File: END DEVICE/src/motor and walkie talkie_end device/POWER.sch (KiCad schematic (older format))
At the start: 65 parts, among them IC2 BQ24616RGER, J4 Barrel_Jack_Switch, J5 Motor_Out, J6 BATT_CONN, Q1 DMP6185SE, Q2 DMP6185SE, Q3 FQPF7N65C, Q4 IRF540NPBF, Q5 IRF540NPBF, Q6 DMP6185SE, U6 IRS2128SPBF

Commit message: third commit:very minor changes
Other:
- note added: "Power in= 12V/ 18V(>3A)"
- note added: "TERMINATION CURRENT SETPOINT"
- note removed: "Power in= 12V/ 18V(3A)"
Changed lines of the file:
@@
 ISET2
 Text Notes 1050 4550 0    39   Italic 0
-max fast charge currentt=2.5A
+TERMINATION CURRENT SETPOINT
 Text Label 3450 2900 2    39   Italic 0
 ACSET
@@
 	4800 850  4800 700
 Text Notes 700  1700 0    39   Italic 0
-Power in= 12V/ 18V(3A)
+Power in= 12V/ 18V(>3A)
 $Comp
 L Device:R_US R20

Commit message: commit 4:minor changes
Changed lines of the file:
@@
-	0    1    1    0
-$EndComp
-Wire Wire Line
-	3100 2250 3250 2250
-$Comp
-L power:GND #PWR?
-U 1 1 6185AE66
-P 3100 2250
-AR Path="/6185AE66" Ref="#PWR?"  Part="1"
-AR Path="/615FCEB9/6185AE66" Ref="#PWR0154"  Part="1"
-AR Path="/61DE992E/6185AE66" Ref="#PWR?"  Part="1"
-F 0 "#PWR0154" H 3100 2000 50  0001 C CNN
-F 1 "GND" H 3105 2077 50  0000 C CNN
-F 2 "" H 3100 2250 50  0001 C CNN
-F 3 "" H 3100 2250 50  0001 C CNN
-	1    3100 2250
 	0    1    1    0
 $EndComp
@@
 	1    0    0    -1
 $EndComp
-Wire Wire Line
-	4800 850  4800 700
 Text Notes 700  1700 0    39   Italic 0
 Power in= 12V/ 18V(>3A)
@@
 Text GLabel 9150 1300 2    50   Input ~ 10
 TO_SYS
+Wire Wire Line
+	4800 700  4800 850
+$Comp
+L power:PWR_FLAG #FLG0105
+U 1 1 62374A60
+P 4800 1400
+F 0 "#FLG0105" H 4800 1475 50  0001 C CNN
+F 1 "PWR_FLAG" H 4500 1600 50  0000 L CNN
+F 2 "" H 4800 1400 50  0001 C CNN
+F 3 "~" H 4800 1400 50  0001 C CNN
+	1    4800 1400
+	0    -1   -1   0
+$EndComp
+Wire Wire Line
+	2400 2250 2400 1950
+Wire Wire Line
+	2400 1950 1850 1950
+Wire Wire Line
+	2400 2250 3250 2250
 $EndSCHEMATC

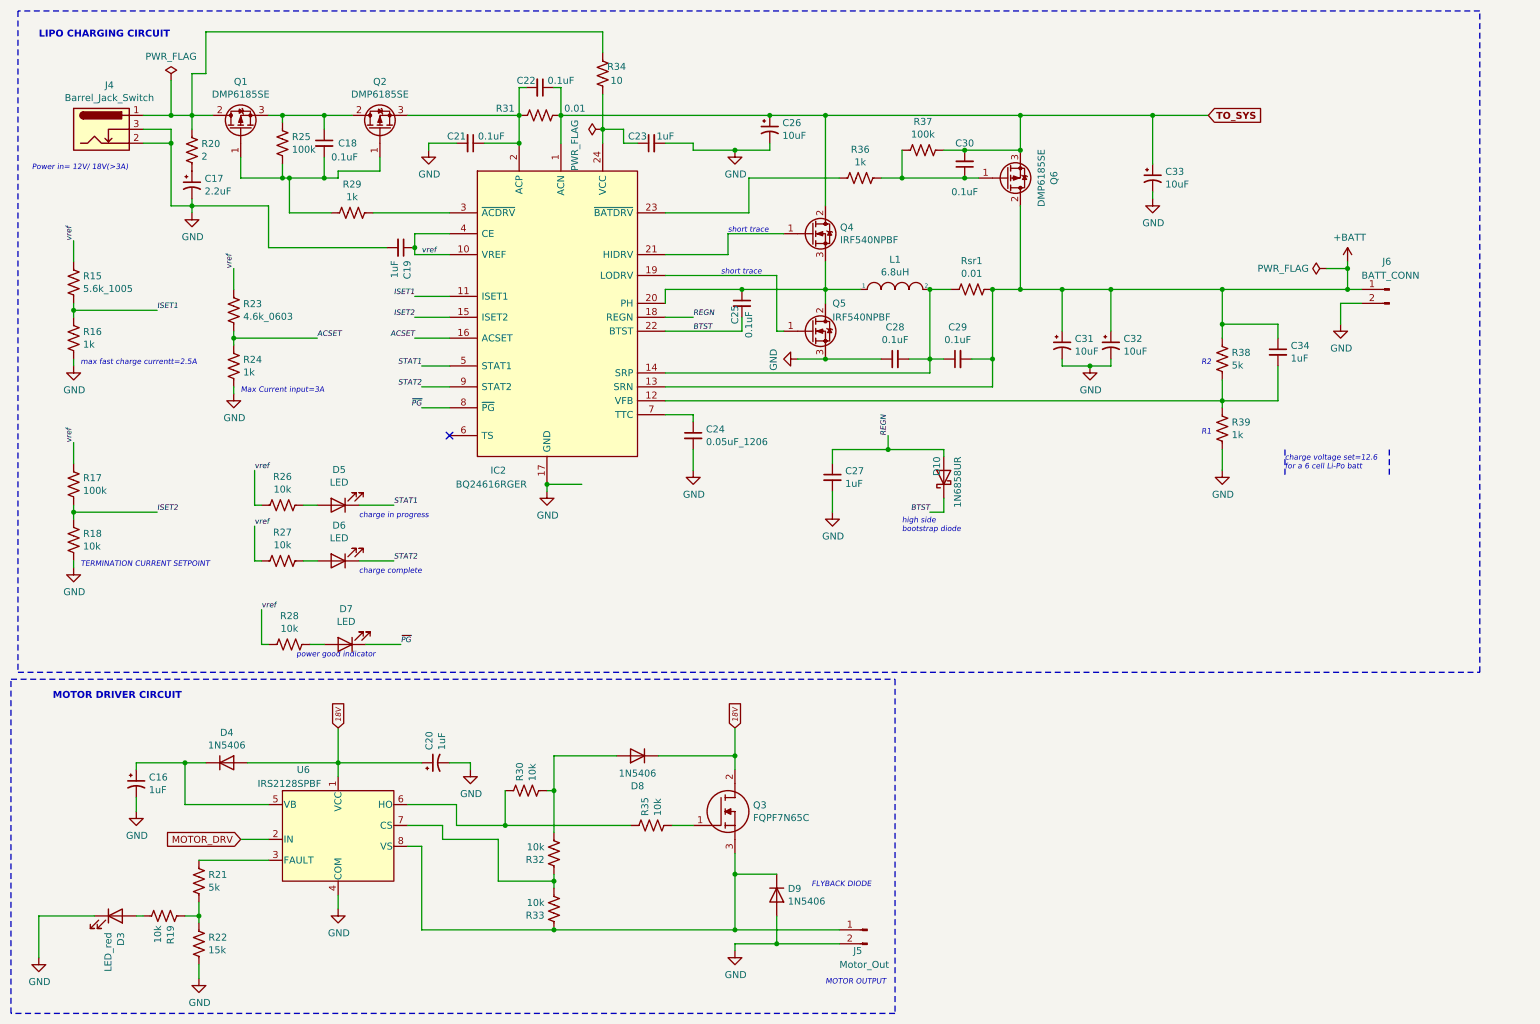
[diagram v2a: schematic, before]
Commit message: All footprint associations updated
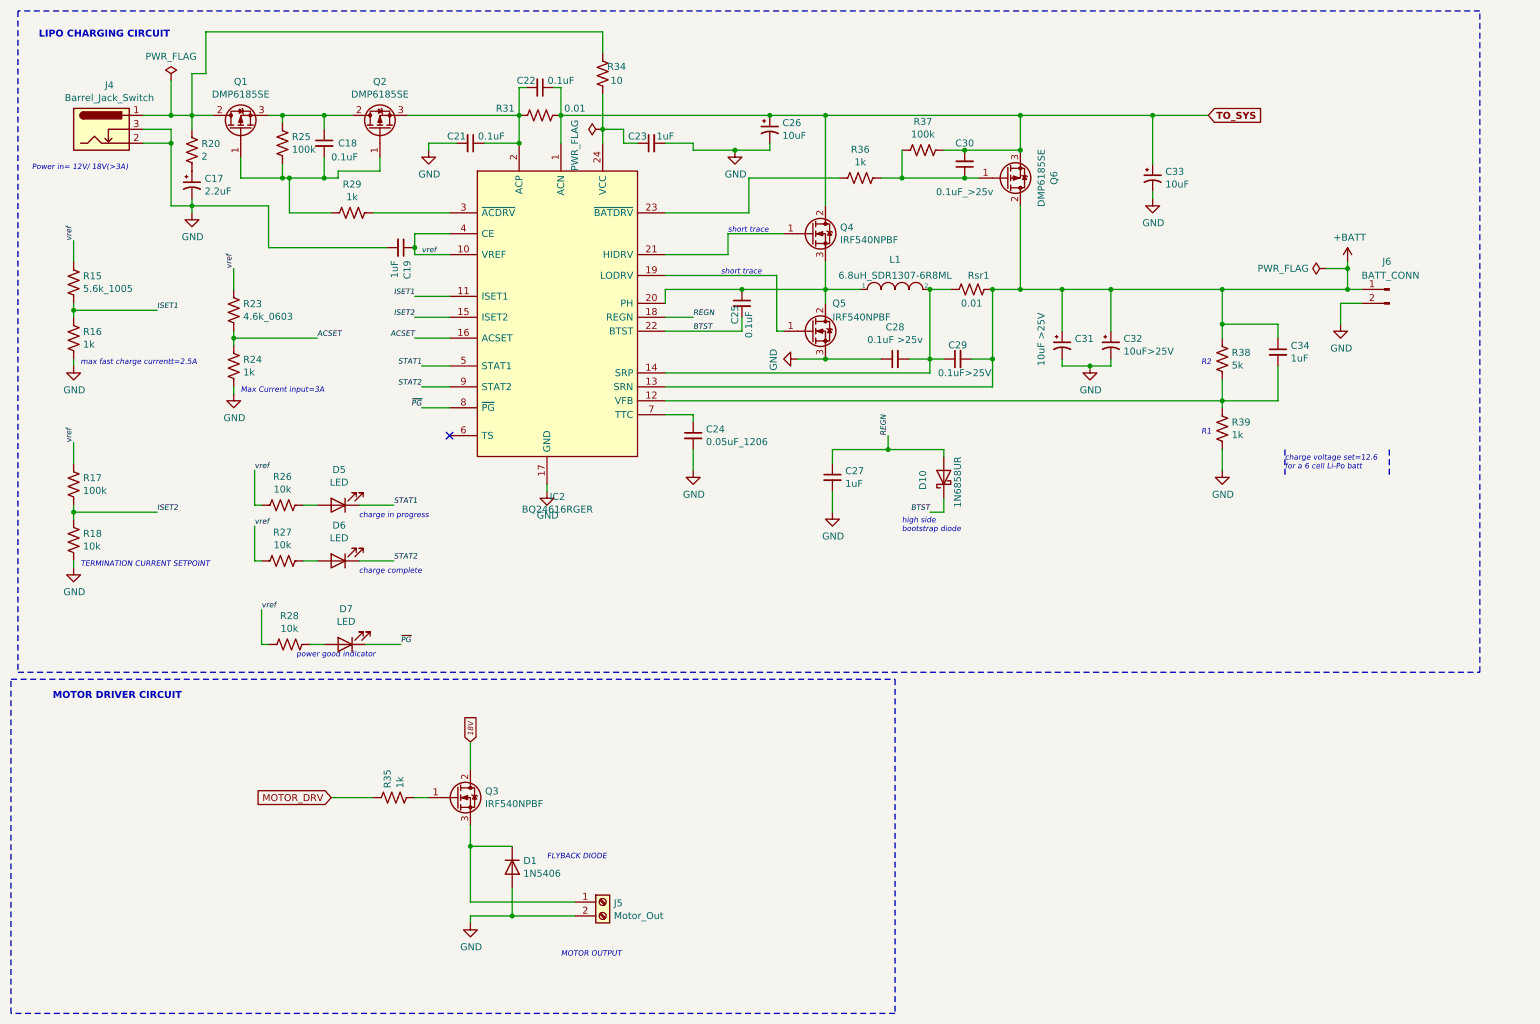
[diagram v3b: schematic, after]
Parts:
- removed C16, C20: 1uF, symbol Device:CP1_Small
- removed D3: LED_red, symbol Device:LED
- removed D4, D8, D9: 1N5406, Diode_THT:D_DO-201AD_P15.24mm_Horizontal, symbol Diode:1N5406
- removed J5: Motor_Out, symbol Connector:Conn_01x02_Male
- removed Q3: FQPF7N65C, TO254P490X1016X1990-3P, symbol SamacSys_Parts:FQPF7N65C
- removed R19, R30, R32, R33: 10k, symbol Device:R_US
- removed R21: 5k, symbol Device:R_US
- removed R22: 15k, symbol Device:R_US
- removed U6: IRS2128SPBF, symbol remote_devices:IRS2128SPBF
- added D1: 1N5406, Diode_THT:D_DO-201AD_P15.24mm_Horizontal, symbol Diode:1N5406
- added J5: Motor_Out, TerminalBlock:TerminalBlock_Altech_AK300-2_P5.00mm, symbol Connector:Screw_Terminal_01x02
- added Q3: IRF540NPBF, Package_TO_SOT_THT:TO-220-3_Vertical, symbol Transistor_FET:IRF540N
- C17, C26, C33: footprint (none) -> Capacitor_Tantalum_SMD:CP_EIA-2012-12_Kemet-R
- C18, C19, C21, C22, C23, C24, C25, C27, C34: footprint (none) -> Capacitor_SMD:C_0603_1608Metric
- C28: value 0.1uF -> 0.1uF >25v; footprint (none) -> Capacitor_SMD:C_0603_1608Metric
- C29: value 0.1uF -> 0.1uF>25V; footprint (none) -> Capacitor_SMD:C_0603_1608Metric
- C30: value 0.1uF -> 0.1uF_>25v; footprint (none) -> Capacitor_SMD:C_0603_1608Metric
- C31: value 10uF -> 10uF >25V; footprint (none) -> Capacitor_Tantalum_SMD:CP_EIA-1608-10_AVX-L
- C32: value 10uF -> 10uF>25V; footprint (none) -> Capacitor_Tantalum_SMD:CP_EIA-1608-10_AVX-L
- D5, D6, D7: footprint (none) -> LED_SMD:LED_0603_1608Metric
- IC2: footprint QFN50P400X400X100-25N-D -> Package_DFN_QFN:QFN-24-1EP_4x4mm_P0.5mm_EP2.6x2.6mm_ThermalVias
- J4: footprint (none) -> Connector_BarrelJack:BarrelJack_Horizontal
- J6: footprint (none) -> Connector_JST:JST_PH_B2B-PH-K_1x02_P2.00mm_Vertical
- L1: value 6.8uH -> 6.8uH_SDR1307-6R8ML; footprint (none) -> Remote_devices:SDR1307680KL
- Q1, Q2, Q6: footprint Package_SON:Diodes_PowerDI3333-8 -> Package_TO_SOT_SMD:SOT-223
- R15: footprint (none) -> Resistor_SMD:R_0402_1005Metric_Pad0.72x0.64mm_HandSolder
- R16, R17, R18, R20, R23, R24, R25, R26, R27, R28, R29, R31, R34, R36, R37, R38, R39, Rsr1: footprint (none) -> Resistor_SMD:R_0603_1608Metric
- R35: value 10k -> 1k; footprint (none) -> Resistor_SMD:R_0603_1608Metric
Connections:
- net 18V: now also Q3.2 (D)
- net GND: now also D1.2 (A), J5.2 (Pin_2)
- net MOTOR_DRV: now also R35.2
- net at R35.1: now also Q3.1 (G)
- new net: D1.1 (K), J5.1 (Pin_1), Q3.3 (S)
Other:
- moved on the sheet: R35

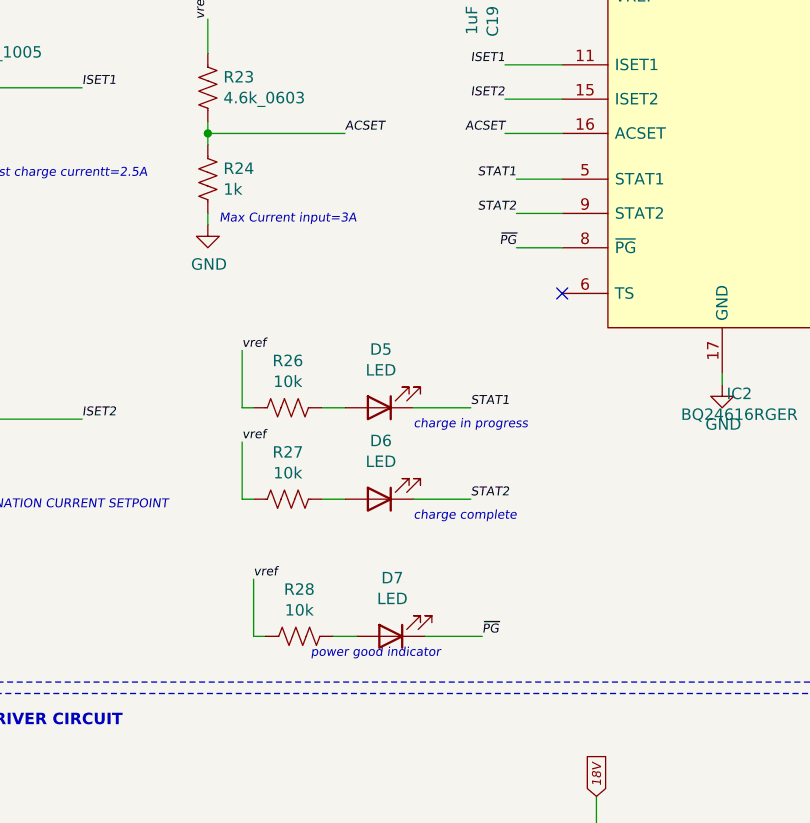
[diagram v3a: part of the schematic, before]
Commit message: Version 2 compressed board
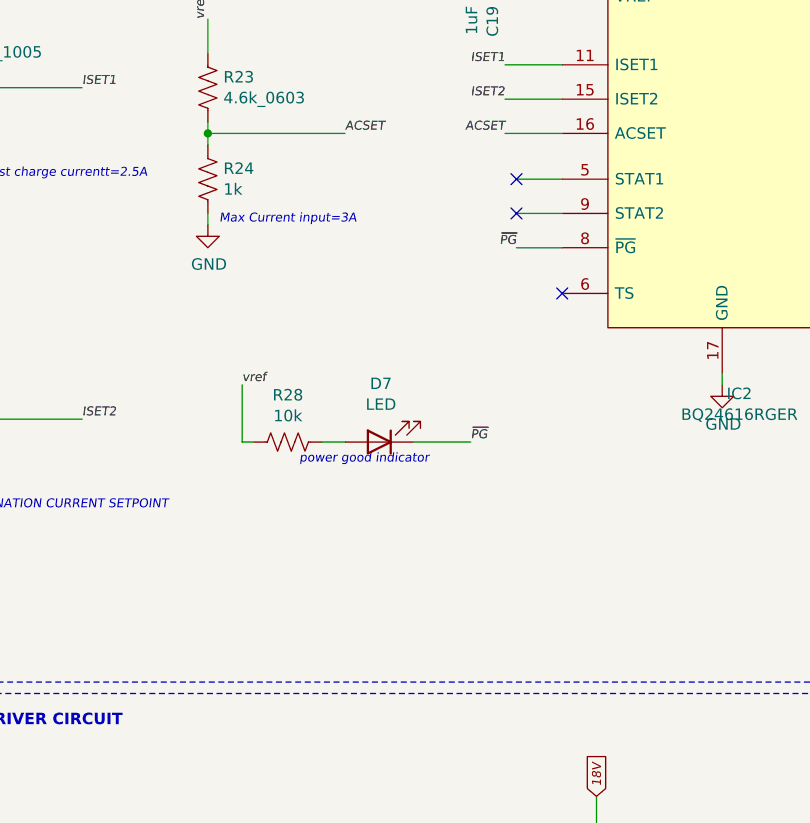
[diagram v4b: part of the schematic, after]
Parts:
- removed D5, D6: LED, LED_SMD:LED_0603_1608Metric, symbol Device:LED
- removed R26, R27: 10k, Resistor_SMD:R_0603_1608Metric, symbol Device:R_US
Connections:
- net STAT1: no longer names the net of IC2.5 (STAT1)
- net STAT2: no longer names the net of IC2.9 (STAT2)
- no-connect marks 1 -> 3
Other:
- note removed: "charge complete"
- note removed: "charge in progress"
- moved on the sheet: D7, R28
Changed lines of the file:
@@
 Text Label 3500 2300 0    39   Italic 0
 vref
-Text Label 2350 4850 0    39   Italic 0
+Text Label 2300 4000 0    39   Italic 0
 vref
 $Comp
 L Device:R_US R28
 U 1 1 617905B6
-P 2550 5100
+P 2500 4250
 AR Path="/615FCEB9/617905B6" Ref="R28"  Part="1"
 AR Path="/61DE992E/617905B6" Ref="R?"  Part="1"
-F 0 "R28" V 2345 5100 50  0000 C CNN
-F 1 "10k" V 2436 5100 50  0000 C CNN
-F 2 "Resistor_SMD:R_0603_1608Metric" V 2590 5090 50  0001 C CNN
-F 3 "~" H 2550 5100 50  0001 C CNN
-	1    2550 5100
+F 0 "R28" V 2295 4250 50  0000 C CNN
+F 1 "10k" V 2386 4250 50  0000 C CNN
+F 2 "Resistor_SMD:R_0603_1608Metric" V 2540 4240 50  0001 C CNN
+F 3 "~" H 2500 4250 50  0001 C CNN
+	1    2500 4250
 	0    1    1    0
 $EndComp
 Wire Wire Line
-	2350 4850 2350 5100
-Wire Wire Line
-	2350 5100 2400 5100
+	2300 4000 2300 4250
+Wire Wire Line
+	2300 4250 2350 4250
 $Comp
 L Device:LED D7
 U 1 1 61799560
-P 2950 5100
+P 2900 4250
 AR Path="/615FCEB9/61799560" Ref="D7"  Part="1"
 AR Path="/61DE992E/61799560" Ref="D?"  Part="1"
-F 0 "D7" H 2943 4845 50  0000 C CNN
-F 1 "LED" H 2943 4936 50  0000 C CNN
-F 2 "LED_SMD:LED_0603_1608Metric" H 2950 5100 50  0001 C CNN
-F 3 "~" H 2950 5100 50  0001 C CNN
-	1    2950 5100
+F 0 "D7" H 2893 3995 50  0000 C CNN
+F 1 "LED" H 2893 4086 50  0000 C CNN
+F 2 "LED_SMD:LED_0603_1608Metric" H 2900 4250 50  0001 C CNN
+F 3 "~" H 2900 4250 50  0001 C CNN
+	1    2900 4250
 	-1   0    0    1
 $EndComp
 Wire Wire Line
-	3350 5100 3100 5100
-Wire Wire Line
-	2800 5100 2700 5100
-Text Notes 2600 5200 0    39   Italic 0
+	3300 4250 3050 4250
+Wire Wire Line
+	2750 4250 2650 4250
+Text Notes 2550 4350 0    39   Italic 0
 power good indicator
 Text Label 3500 3400 2    39   Italic 0
@@
 Wire Wire Line
 	3700 3400 3500 3400
-Text Label 3350 5100 0    39   Italic 0
+Text Label 3300 4250 0    39   Italic 0
 ~PG
 $Comp
@@
 Wire Wire Line
 	7600 3050 7600 2550
-Text Label 2300 4250 0    39   Italic 0
-vref
-$Comp
-L Device:R_US R27
-U 1 1 617F4055
-P 2500 4500
-AR Path="/615FCEB9/617F4055" Ref="R27"  Part="1"
-AR Path="/61DE992E/617F4055" Ref="R?"  Part="1"
-F 0 "R27" V 2295 4500 50  0000 C CNN
-F 1 "10k" V 2386 4500 50  0000 C CNN
-F 2 "Resistor_SMD:R_0603_1608Metric" V 2540 4490 50  0001 C CNN
-F 3 "~" H 2500 4500 50  0001 C CNN
-	1    2500 4500
-	0    1    1    0
-$EndComp
-Wire Wire Line
-	2300 4250 2300 4500
-Wire Wire Line
-	2300 4500 2350 4500
-$Comp
-L Device:LED D6
-U 1 1 617F4061
-P 2900 4500
-AR Path="/615FCEB9/617F4061" Ref="D6"  Part="1"
-AR Path="/61DE992E/617F4061" Ref="D?"  Part="1"
-F 0 "D6" H 2893 4245 50  0000 C CNN
-F 1 "LED" H 2893 4336 50  0000 C CNN
-F 2 "LED_SMD:LED_0603_1608Metric" H 2900 4500 50  0001 C CNN
-F 3 "~" H 2900 4500 50  0001 C CNN
-	1    2900 4500
-	-1   0    0    1
-$EndComp
-Wire Wire Line
-	3300 4500 3050 4500
-Wire Wire Line
-	2750 4500 2650 4500
-Text Label 3300 4500 0    39   Italic 0
-STAT2
-Text Label 2300 3850 0    39   Italic 0
-vref
-$Comp
-L Device:R_US R26
-U 1 1 617FAE61
-P 2500 4100
-AR Path="/615FCEB9/617FAE61" Ref="R26"  Part="1"
-AR Path="/61DE992E/617FAE61" Ref="R?"  Part="1"
-F 0 "R26" V 2295 4100 50  0000 C CNN
-F 1 "10k" V 2386 4100 50  0000 C CNN
-F 2 "Resistor_SMD:R_0603_1608Metric" V 2540 4090 50  0001 C CNN
-F 3 "~" H 2500 4100 50  0001 C CNN
-	1    2500 4100
-	0    1    1    0
-$EndComp
-Wire Wire Line
-	2300 3850 2300 4100
-Wire Wire Line
-	2300 4100 2350 4100
-$Comp
-L Device:LED D5
-U 1 1 617FAE6D
-P 2900 4100
-AR Path="/615FCEB9/617FAE6D" Ref="D5"  Part="1"
-AR Path="/61DE992E/617FAE6D" Ref="D?"  Part="1"
-F 0 "D5" H 2893 3845 50  0000 C CNN
-F 1 "LED" H 2893 3936 50  0000 C CNN
-F 2 "LED_SMD:LED_0603_1608Metric" H 2900 4100 50  0001 C CNN
-F 3 "~" H 2900 4100 50  0001 C CNN
-	1    2900 4100
-	-1   0    0    1
-$EndComp
-Wire Wire Line
-	3300 4100 3050 4100
-Wire Wire Line
-	2750 4100 2650 4100
-Text Label 3300 4100 0    39   Italic 0
-STAT1
-Text Notes 3050 4200 0    39   Italic 0
-charge in progress
-Text Notes 3050 4600 0    39   Italic 0
-charge complete
 $Comp
 L Device:C_Small C23
@@
 Text Notes 750  750  0    50   ~ 10
 LIPO CHARGING CIRCUIT
-Text Label 3500 3250 2    39   Italic 0
-STAT2
-Text Label 3500 3100 2    39   Italic 0
-STAT1
 Wire Wire Line
 	3700 3100 3500 3100
@@
 	1    0    0    -1
 $EndComp
+NoConn ~ 3500 3100
+NoConn ~ 3500 3250
 $EndSCHEMATC

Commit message: latest update
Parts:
- L1: value 6.8uH_SDR1307-6R8ML -> 6.8uH_ASPI-7318-6R8M-T; footprint Remote_devices:SDR1307680KL -> Remote_devices:ASPI-7318-6R8M-T
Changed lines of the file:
@@
 AR Path="/61DE992E/616963BA" Ref="L?"  Part="1"
 F 0 "L1" H 6900 2765 50  0000 C CNN
-F 1 "6.8uH_SDR1307-6R8ML" H 6900 2650 50  0000 C CNN
-F 2 "Remote_devices:SDR1307680KL" H 6900 2550 50  0001 C CNN
+F 1 "6.8uH_ASPI-7318-6R8M-T" H 6900 2650 50  0000 C CNN
+F 2 "Remote_devices:ASPI-7318-6R8M-T" H 6900 2550 50  0001 C CNN
 F 3 "~" H 6900 2550 50  0001 C CNN
 	1    6900 2550

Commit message: 90% complete and. PCB done with tracks and design rules verified as well as dimensions
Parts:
- removed D10: 1N6858UR, Diode_SMD:D_MELF, symbol Diode:1N6858UR
- added D4: B320B-13-F, Diode_SMD:D_SMB_Handsoldering, symbol Device:D_Schottky_ALT
- C17: value 2.2uF -> 2.2uF_TCKIX225DT; footprint Capacitor_Tantalum_SMD:CP_EIA-2012-12_Kemet-R -> Capacitor_Tantalum_SMD:CP_EIA-7343-31_Kemet-D; Mfr (none) -> TCKIX225DT; Supplier (none) -> Digikey
- C26, C33: footprint Capacitor_Tantalum_SMD:CP_EIA-2012-12_Kemet-R -> Capacitor_Tantalum_SMD:CP_EIA-6032-28_Kemet-C; Mfr No. (none) -> T491C106K035AT; Supplier (none) -> LCSC
- C31, C32: footprint Capacitor_Tantalum_SMD:CP_EIA-1608-10_AVX-L -> Capacitor_Tantalum_SMD:CP_EIA-6032-28_Kemet-C; Mfr No. (none) -> T491C106K035AT; Supplier (none) -> LCSC
- D1: value 1N5406 -> RS2K-13-F; footprint Diode_THT:D_DO-201AD_P15.24mm_Horizontal -> Diode_SMD:D_SMB_Handsoldering
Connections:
- net BTST: now also D4.1 (K)
- net REGN: now also D4.2 (A)
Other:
- note added: "NB// incase the board is in production already, the Batt+ track can be cut \nand also the TO-SYS line can be removed(from the p-channel mosfet side) \nand rerouted manually to the sitch number 2."
- moved on the sheet: C27, D7, R15, R16, R17, R18, R23, R24, R28
